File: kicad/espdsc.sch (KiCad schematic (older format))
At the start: 14 parts, among them J1 RJ45, P1 USB_B, SW1 Reset, SW2 Prog, U1 ESP-12E, U2 MCP1825S-3302E/DB, U3 TXB0104

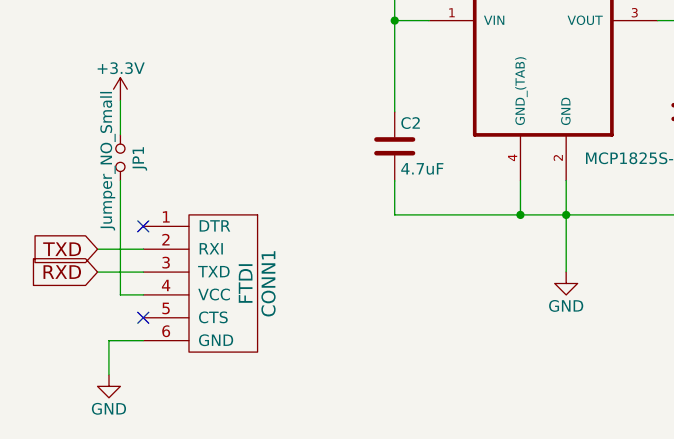
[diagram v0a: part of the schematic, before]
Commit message: update design for v1.0 release
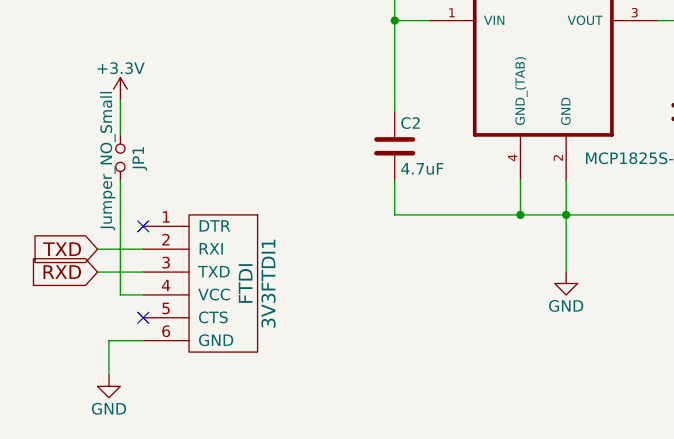
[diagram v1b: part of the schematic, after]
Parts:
- renumbered CONN1 to 3V3FTDI1
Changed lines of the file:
@@
 $EndComp
 $Comp
-L FTDI CONN1
+L FTDI 3V3FTDI1
 U 1 1 58B249EE
 P 3150 6650
-F 0 "CONN1" H 3250 7000 60  0000 C CNN
+F 0 "3V3FTDI1" H 3250 7000 60  0000 C CNN
 F 1 "FTDI" H 3250 6900 60  0000 C CNN
 F 2 "synfinatic:FTDIHeader" H 3150 6650 60  0001 C CNN
@@
 $EndComp
 $Comp
-L GND #PWR01
+L GND #PWR11
 U 1 1 58B24D32
 P 8150 5850
-F 0 "#PWR01" H 8150 5600 50  0001 C CNN
+F 0 "#PWR11" H 8150 5600 50  0001 C CNN
 F 1 "GND" H 8150 5700 50  0000 C CNN
 F 2 "" H 8150 5850 50  0000 C CNN
@@
 $EndComp
 $Comp
-L +5V #PWR02
+L +5V #PWR10
 U 1 1 58B24D4F
 P 7900 5000
-F 0 "#PWR02" H 7900 4850 50  0001 C CNN
+F 0 "#PWR10" H 7900 4850 50  0001 C CNN
 F 1 "+5V" H 7900 5140 50  0000 C CNN
 F 2 "" H 7900 5000 50  0000 C CNN
@@
 $EndComp
 $Comp
-L GND #PWR03
+L GND #PWR13
 U 1 1 58B2504E
 P 8900 3800
-F 0 "#PWR03" H 8900 3550 50  0001 C CNN
+F 0 "#PWR13" H 8900 3550 50  0001 C CNN
 F 1 "GND" H 8900 3650 50  0000 C CNN
 F 2 "" H 8900 3800 50  0000 C CNN
@@
 $EndComp
 $Comp
-L +5V #PWR04
+L +5V #PWR12
 U 1 1 58B25071
 P 8800 2400
-F 0 "#PWR04" H 8800 2250 50  0001 C CNN
+F 0 "#PWR12" H 8800 2250 50  0001 C CNN
 F 1 "+5V" H 8800 2540 50  0000 C CNN
 F 2 "" H 8800 2400 50  0000 C CNN
@@
 NoConn ~ 2950 6500
 $Comp
-L GND #PWR05
+L GND #PWR1
 U 1 1 58B257DE
 P 2800 7150
-F 0 "#PWR05" H 2800 6900 50  0001 C CNN
+F 0 "#PWR1" H 2800 6900 50  0001 C CNN
 F 1 "GND" H 2800 7000 50  0000 C CNN
 F 2 "" H 2800 7150 50  0000 C CNN
@@
 $EndComp
 $Comp
-L GND #PWR06
+L GND #PWR5
 U 1 1 58B2638F
 P 4500 4250
-F 0 "#PWR06" H 4500 4000 50  0001 C CNN
+F 0 "#PWR5" H 4500 4000 50  0001 C CNN
 F 1 "GND" H 4500 4100 50  0000 C CNN
 F 2 "" H 4500 4250 50  0000 C CNN
@@
 $EndComp
 $Comp
-L +3.3V #PWR07
+L +3.3V #PWR3
 U 1 1 58B26ADA
 P 3150 1900
-F 0 "#PWR07" H 3150 1750 50  0001 C CNN
+F 0 "#PWR3" H 3150 1750 50  0001 C CNN
 F 1 "+3.3V" H 3150 2040 50  0000 C CNN
 F 2 "" H 3150 1900 50  0000 C CNN
@@
 $EndComp
 $Comp
-L GND #PWR08
+L GND #PWR9
 U 1 1 58B2724B
 P 6600 3550
-F 0 "#PWR08" H 6600 3300 50  0001 C CNN
+F 0 "#PWR9" H 6600 3300 50  0001 C CNN
 F 1 "GND" H 6600 3400 50  0000 C CNN
 F 2 "" H 6600 3550 50  0000 C CNN
@@
 $EndComp
 $Comp
-L +3.3V #PWR09
+L +3.3V #PWR8
 U 1 1 58B27454
 P 6550 2400
-F 0 "#PWR09" H 6550 2250 50  0001 C CNN
+F 0 "#PWR8" H 6550 2250 50  0001 C CNN
 F 1 "+3.3V" H 6550 2540 50  0000 C CNN
 F 2 "" H 6550 2400 50  0000 C CNN
@@
 Connection ~ 3150 2600
 $Comp
-L PWR_FLAG #FLG010
+L PWR_FLAG #FLG1
 U 1 1 58B284AC
 P 6000 6350
-F 0 "#FLG010" H 6000 6445 50  0001 C CNN
+F 0 "#FLG1" H 6000 6445 50  0001 C CNN
 F 1 "PWR_FLAG" H 6000 6530 50  0000 C CNN
 F 2 "" H 6000 6350 50  0000 C CNN
@@
 $EndComp
 $Comp
-L GND #PWR011
+L GND #PWR6
 U 1 1 58B28A76
 P 4800 6700
-F 0 "#PWR011" H 4800 6450 50  0001 C CNN
+F 0 "#PWR6" H 4800 6450 50  0001 C CNN
 F 1 "GND" H 4800 6550 50  0000 C CNN
 F 2 "" H 4800 6700 50  0000 C CNN
@@
 $EndComp
 $Comp
-L +3.3V #PWR012
+L +3.3V #PWR7
 U 1 1 58B28AAB
 P 5350 5400
-F 0 "#PWR012" H 5350 5250 50  0001 C CNN
+F 0 "#PWR7" H 5350 5250 50  0001 C CNN
 F 1 "+3.3V" H 5350 5540 50  0000 C CNN
 F 2 "" H 5350 5400 50  0000 C CNN
@@
 Connection ~ 5350 6450
 $Comp
-L +5V #PWR013
+L +5V #PWR4
 U 1 1 58B3487E
 P 4050 5400
-F 0 "#PWR013" H 4050 5250 50  0001 C CNN
+F 0 "#PWR4" H 4050 5250 50  0001 C CNN
 F 1 "+5V" H 4050 5540 50  0000 C CNN
 F 2 "" H 4050 5400 50  0000 C CNN
@@
 	2950 7000 2800 7000
 $Comp
-L +3.3V #PWR014
+L +3.3V #PWR2
 U 1 1 58B37209
 P 2850 5950
-F 0 "#PWR014" H 2850 5800 50  0001 C CNN
+F 0 "#PWR2" H 2850 5800 50  0001 C CNN
 F 1 "+3.3V" H 2850 6090 50  0000 C CNN
 F 2 "" H 2850 5950 50  0000 C CNN

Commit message: v1.1 board & code
- Move GPIO2/15 to GPIO14/12 to avoid boot conflict
- Remove level shifter and replace with 4x 150Ohm resistors
- Tweak RJ45 footprint for better fit
- Add pullup for D+ on USB
- Remove 3.3V FTDI jumper
- Move Reset button label
- FTDI no longer can provide power
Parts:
- removed JP1: Jumper_NO_Small, Pin_Headers:Pin_Header_Straight_1x02, symbol Jumper_NO_Small
- removed U3: TXB0104, Housings_SOIC:SOIC-14_3.9x8.7mm_Pitch1.27mm, symbol TXB0104
- added R1: 4.7k, Resistors_SMD:R_0805_HandSoldering, symbol R
- added R2: 1.5k, Resistors_SMD:R_0805_HandSoldering, symbol R
- added R5: 1k, Resistors_SMD:R_0805_HandSoldering, symbol R
- added R6, R7, R8, R9: 510, Resistors_SMD:R_0805_HandSoldering, symbol R
- J1: footprint Connectors:RJ45_8 -> synfinatic:RJ45_8
- P1: symbol USB_B -> USB_B-RESCUE-espdsc
- SW1, SW2: symbol SW_SPST -> SW_SPST-RESCUE-espdsc
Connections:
- net +3V3: now also R2.1, R5.1
- net GND: now also R1.2
- net at U1.10 (GPIO15): now also R1.1
- net at U1.11 (GPIO2): now also R5.2
- net at U1.13 (GPIO4): now also R9.2
- net at U1.14 (GPIO5): now also R7.2
- net at U1.5 (GPIO14): now also R8.2
- net at U1.6 (GPIO12): now also R6.2
- net at J1.1: now also R6.1
- net at J1.3: now also R8.1
- net at J1.5: now also R9.1
- net at J1.7: now also R7.1
- net at P1.3 (D+): now also R2.2
- no-connect marks 16 -> 15
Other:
- moved on the sheet: SW2

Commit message: v1.2
- Switch ESP12E to pure SMD footprint
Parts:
- U1: footprint ESP8266:ESP-12E -> synfinatic:ESP-12E-SMD
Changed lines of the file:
@@
 EESchema Schematic File Version 2
 LIBS:power
-LIBS:device
-LIBS:transistors
-LIBS:conn
-LIBS:linear
-LIBS:regul
-LIBS:74xx
-LIBS:cmos4000
-LIBS:adc-dac
-LIBS:memory
-LIBS:microcontrollers
-LIBS:dsp
-LIBS:microchip
-LIBS:analog_switches
-LIBS:motorola
-LIBS:texas
-LIBS:intel
-LIBS:audio
-LIBS:interface
-LIBS:digital-audio
-LIBS:philips
-LIBS:display
-LIBS:siliconi
-LIBS:opto
-LIBS:atmel
-LIBS:contrib
-LIBS:ftdi
-LIBS:Power_Management
-LIBS:switches
-LIBS:synfinatic
-LIBS:ESP8266
 LIBS:espdsc-cache
 EELAYER 25 0
@@
 Sheet 1 1
 Title ""
-Date "2017-12-02"
-Rev "v1.1"
+Date "2017-12-03"
+Rev "v1.2"
 Comp "Aaron Turner <synfinatic@gmail.com>"
 Comment1 "https://synfin.net/espdsc"
@@
 F 0 "U1" H 4700 2800 50  0000 C CNN
 F 1 "ESP-12E" H 4700 3000 50  0000 C CNN
-F 2 "ESP8266:ESP-12E" H 4700 2900 50  0001 C CNN
+F 2 "synfinatic:ESP-12E-SMD" H 4700 2900 50  0001 C CNN
 F 3 "" H 4700 2900 50  0001 C CNN
 	1    4700 2900
